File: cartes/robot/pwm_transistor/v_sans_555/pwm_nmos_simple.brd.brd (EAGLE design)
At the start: 32.1 x 31.7 mm, 19 parts

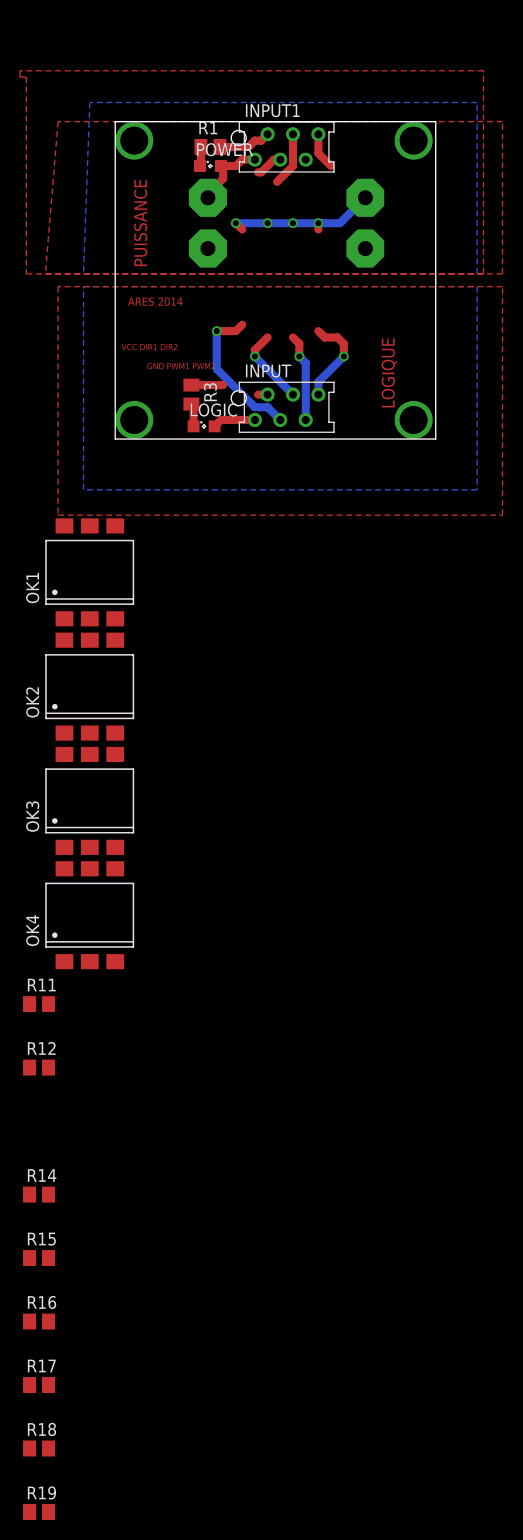
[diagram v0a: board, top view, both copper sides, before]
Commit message: nouvelle carte sans ne555
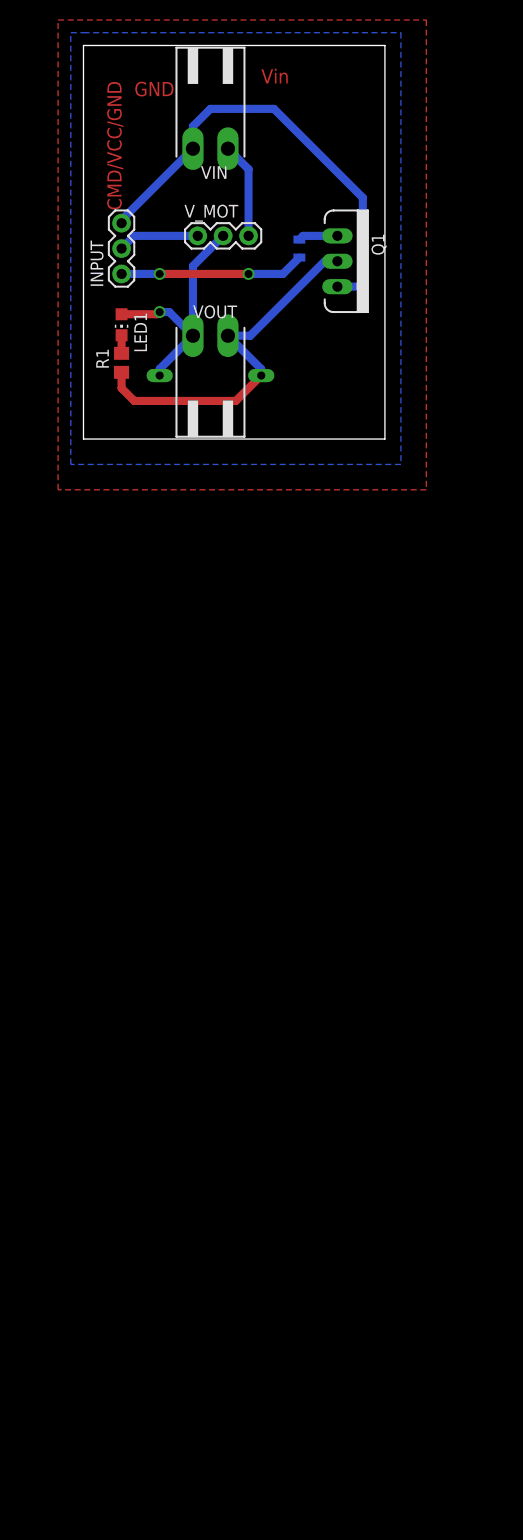
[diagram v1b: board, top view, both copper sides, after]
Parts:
- removed F3: (no value), fuse:SHK20Q
- removed INPUT1: MMATCH-6-, jt-con-micromatch:AMP-215079-6
- removed LOGIC, POWER: (no value), led:SML0805
- removed OK1, OK2, OK3, OK4: 4N25SM, optocoupler:DIL6-SMD
- removed R11, R12, R14, R15, R3: 1k, rcl:M0805
- removed R16, R17, R18, R19: 470, rcl:M0805
- added D1: 1N821, diode:DO35Z10
- added LED1: (no value), led:CHIP-LED0805
- added Q1: MOSFET-NCHANNELFQP30N06L, SparkFun-DiscreteSemi:TO220V
- added R2: 10ohm, SparkFun-Resistors:0805
- added VIN, VOUT: (no value), con-weidmueller-sl35:90-2
- added V_MOT: (no value), SparkFun-Connectors:1X03
- INPUT: value MMATCH-6- -> (none); device jt-con-micromatch:AMP-215079-6 -> SparkFun-Electromechanical:1X03
- R1: value 1k -> (none); device rcl:M0805 -> rcl:R0805
- moved R1 23.3 mm to (3.81, 7.62), turned to 90 degrees
- moved INPUT 19.8 mm to (3.81, 16.5), turned to 90 degrees
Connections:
- removed net +5V: F3.2A, INPUT1.1, POWER.A
- removed net C_DIR1: INPUT.3
- removed net C_DIR2: INPUT.5, OK3.1
- removed net C_PWM1: INPUT.4, OK2.1
- removed net C_PWM2: INPUT.6, OK4.1
- removed net DIR1: INPUT1.3, R16.1
- removed net DIR2: INPUT1.5, R18.1
- removed net FUSE_5V: F3.1A
- removed net GNDA: INPUT1.2, R1.2
- removed net N$1: OK1.2, R11.1
- removed net N$10: OK4.2, R15.1
- removed net N$19: OK1.4, R16.2
- removed net N$20: OK2.4, R17.2
- removed net N$21: OK3.4, R18.2
- removed net N$22: OK4.4, R19.2
- removed net N$4: LOGIC.C, R3.2
- removed net N$9: OK3.2, R14.1
- removed net PWM1: INPUT1.4, R17.1
- removed net PWM2: INPUT1.6, R19.1
- new net 12V: VIN.1, V_MOT.3
- new net CMD: INPUT.1, R2.1
- new net N$5: D1.A, Q1.2, R1.1, VOUT.2
- new net V+_MOT: D1.C, LED1.A, VOUT.1, V_MOT.2
- net GND: now also INPUT.3, Q1.3, VIN.2; no longer INPUT.2, R11.2, R12.2, R14.2, R15.2, R3.1
- net N$2: now also LED1.C, R1.2; no longer OK2.2, R12.1
- net N$3: now also Q1.1, R2.2; no longer POWER.C, R1.1
- net VCC: now also INPUT.2, V_MOT.1; no longer INPUT.1, LOGIC.A
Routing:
- net GND: track 4.12 -> 45.5 mm
- net N$5: track 0.00 -> 36.5 mm, vias 1 -> 0
- net V+_MOT: track 0.00 -> 24.8 mm, vias 0 -> 1
- net CMD: track 0.00 -> 18.5 mm, vias 0 -> 2
- net FUSE_5V: track 15.5 -> 0.00 mm, vias 4 -> 0
- net C_DIR1: track 15.1 -> 0.00 mm, vias 1 -> 0
- net 12V: track 0.00 -> 9.57 mm
- net C_PWM2: track 9.20 -> 0.00 mm, vias 1 -> 0
- net C_DIR2: track 8.78 -> 0.00 mm, vias 1 -> 0
- net C_PWM1: track 7.82 -> 0.00 mm, vias 1 -> 0
- net +5V: track 7.56 -> 0.00 mm
- net PWM1: track 5.42 -> 0.00 mm
- net GNDA: track 5.29 -> 0.00 mm
- net VCC: track 4.29 -> 8.15 mm
- net PWM2: track 3.70 -> 0.00 mm
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- removed copper zone on layer 1, net GNDA
- removed copper zone on layer 16, net GNDA
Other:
- board size 32.1 x 31.7 mm -> 30.1 x 39.4 mm
- board text added: "CMD/VCC/GND"
- board text added: "GND"
- board text added: "Vin"
- board text removed: "ARES 2014"
- board text removed: "GND PWM1 PWM2"
- board text removed: "LOGIQUE"
- board text removed: "PUISSANCE"
- board text removed: "VCC DIR1 DIR2"
